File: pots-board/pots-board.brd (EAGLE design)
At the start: 160 x 100 mm, 29 parts

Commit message: mods
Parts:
- renumbered A to POT1, B to POT2, C to POT3, D to POT4, E to POT5
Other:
- board text added: "hotchk155"
- board text added: "meta-step pots board rev 1"
- board text added: "six4pix.com/metastep"

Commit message: reverse order
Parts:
- moved VCC 125.1 mm to (14.0, 61.0)
- moved GND 124.5 mm to (14.0, 43.2)
- moved GND40 124.5 mm to (14.0, 45.7)
- moved VA 124.5 mm to (14.0, 58.4)
- moved VB 124.5 mm to (14.0, 55.9)
- moved VC 124.5 mm to (14.0, 53.3)
- moved VD 124.5 mm to (14.0, 50.8)
- moved VE 124.5 mm to (14.0, 48.3)
- moved VC1 12.7 mm to (16.5, 61.0)
- moved VCC10 12.7 mm to (135.9, 61.0)
- moved XD 2.54 mm to (16.5, 50.8)
- moved YD 2.54 mm to (135.9, 50.8)
- moved XA 2.54 mm to (16.5, 58.4)
- moved XB 2.54 mm to (16.5, 55.9)
- moved XC 2.54 mm to (16.5, 53.3)
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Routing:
- net N$3: track 139.5 -> 14.8 mm, vias 2 -> 0
- net N$7: track 42.7 -> 127.3 mm, vias 2 -> 1
- net N$4: track 112.9 -> 42.6 mm
- net N$1: track 189.1 -> 136.5 mm, vias 5 -> 0
- net N$6: track 59.9 -> 100.8 mm, vias 2 -> 1
- net N$5: track 85.3 -> 67.2 mm, vias 2 -> 1
- net N$10: track 119.4 -> 121.8 mm, vias 0 -> 1
- net N$8: track 122.5 -> 120.1 mm
- net GND: track 1.27 -> 0.00 mm
- net N$11: track 121.0 -> 120.4 mm, vias 0 -> 1
- net N$9: track 121.0 -> 120.4 mm
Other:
- outline, holes or cut-outs redrawn
- board text added: "1"
- board text added: "2"
- board text added: "3"
- board text added: "4"
- board text added: "5"
- board text added: "VCC A1 A2 A3 A4 A5 GND GND"
- board text added: "VCC B1 B2 B3 B4 B5 GND GND"

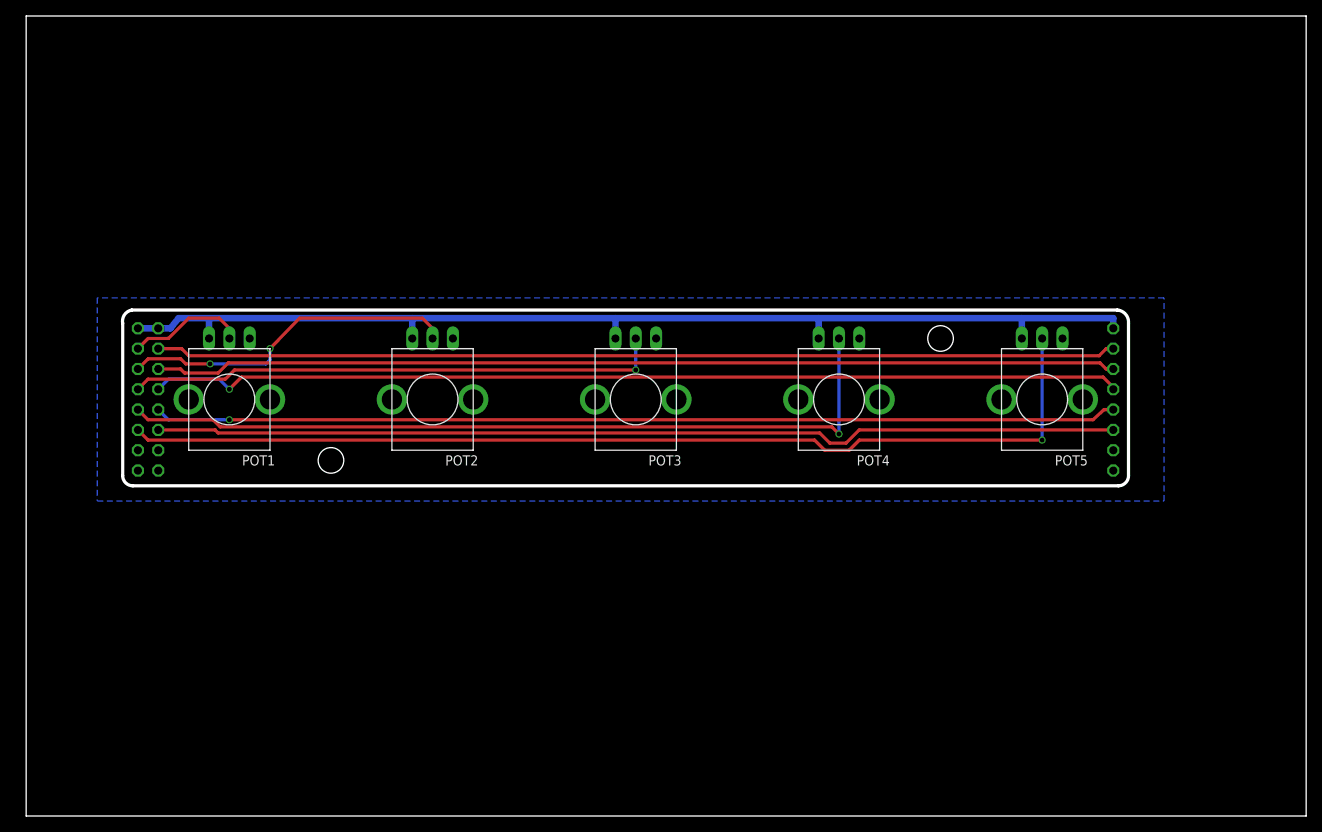
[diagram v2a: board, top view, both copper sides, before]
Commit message: pos
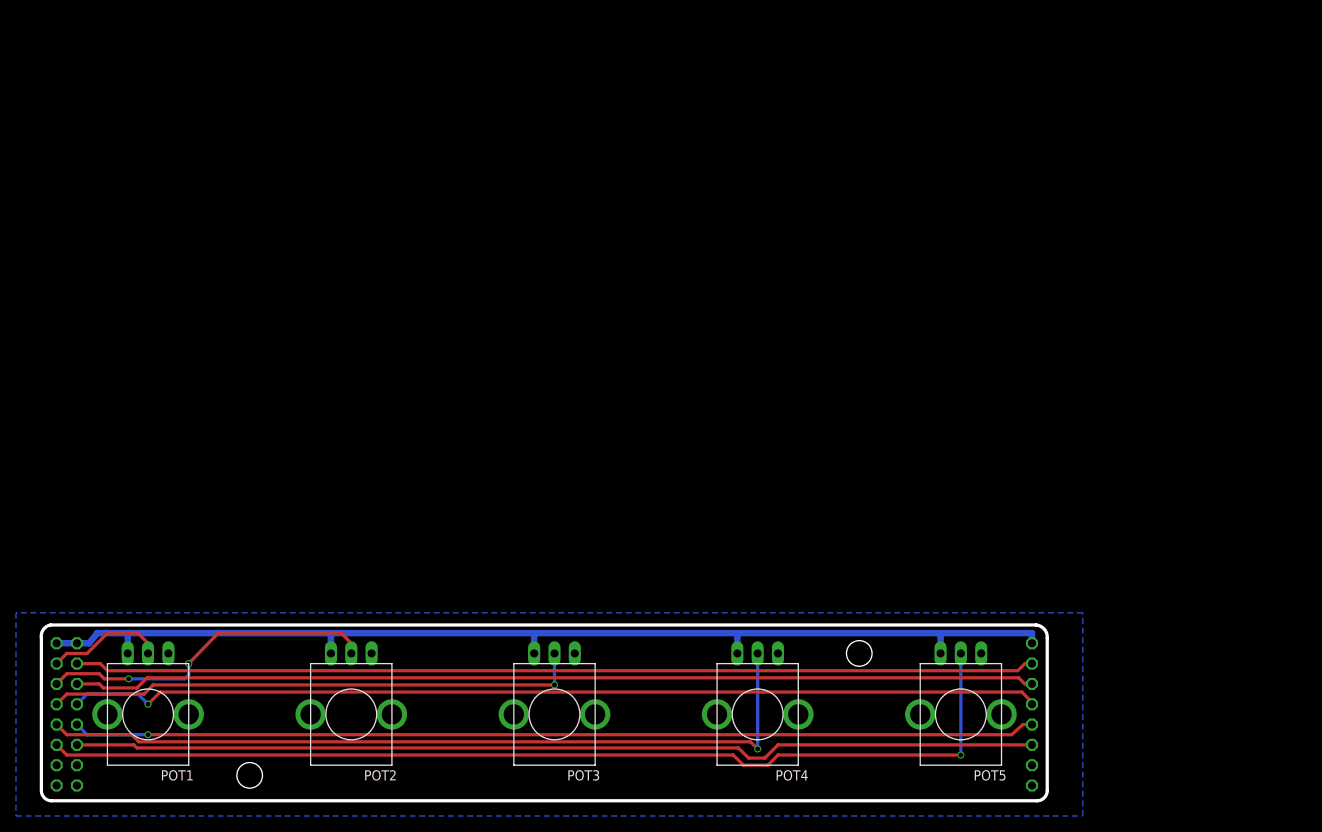
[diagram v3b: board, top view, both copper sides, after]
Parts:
- moved POT1 40.7 mm to (15.2, 12.7)
- moved POT2 40.7 mm to (40.6, 12.7)
- moved POT3 40.7 mm to (66.0, 12.7)
- moved POT4 40.7 mm to (91.4, 12.7)
- moved POT5 40.7 mm to (116.8, 12.7)
- moved VA 40.7 mm to (3.81, 19.1)
- moved VB 40.7 mm to (3.81, 16.5)
- moved VC 40.7 mm to (3.81, 14.0)
- moved VC1 40.7 mm to (6.35, 21.6)
- moved VCC 40.7 mm to (3.81, 21.6)
- moved XA 40.7 mm to (6.35, 19.1)
- moved XB 40.7 mm to (6.35, 16.5)
- moved XC 40.7 mm to (6.35, 14.0)
- moved GD1 40.7 mm to (6.35, 6.35)
- moved GD2 40.7 mm to (6.35, 3.81)
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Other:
- board size 160 x 100 mm -> 125.8 x 22 mm

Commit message: stuff
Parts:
- added C1, C2, C3, C4: (no value), rcl:C0805
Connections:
- removed net N$1: POT1.B, POT2.B, POT3.B, POT4.B, POT5.B, VC1.1, VCC.1, VCC10.1
- new net VCC: C1.1, C2.1, C3.1, C4.1, POT1.B, POT2.B, POT3.B, POT4.B, POT5.B, VC1.1, VCC.1, VCC10.1
- net GND: now also C1.2, C2.2, C3.2, C4.2
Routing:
- net VCC: track 0.00 -> 147.9 mm
- net N$1: track 136.5 -> 0.00 mm
- net GND: track 0.00 -> 30.6 mm, vias 0 -> 3
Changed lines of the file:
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@@
 <attribute name="VALUE" x="127" y="18.415" size="1.27" layer="28" rot="MR0"/>
+</element>
+<element name="C1" library="rcl" package="C0805" value="" x="34.29" y="20.32" smashed="yes" rot="R180">
+<attribute name="NAME" x="34.671" y="19.05" size="1.27" layer="25" rot="R180"/>
+<attribute name="VALUE" x="35.56" y="22.86" size="1.27" layer="27" rot="R180"/>
+</element>
+<element name="C2" library="rcl" package="C0805" value="" x="59.69" y="20.32" smashed="yes" rot="R180">
+<attribute name="NAME" x="59.817" y="19.05" size="1.27" layer="25" rot="R180"/>
+<attribute name="VALUE" x="60.96" y="22.86" size="1.27" layer="27" rot="R180"/>
+</element>
+<element name="C3" library="rcl" package="C0805" value="" x="85.09" y="20.32" smashed="yes" rot="R180">
+<attribute name="NAME" x="85.217" y="19.05" size="1.27" layer="25" rot="R180"/>
+<attribute name="VALUE" x="86.36" y="22.86" size="1.27" layer="27" rot="R180"/>
+</element>
+<element name="C4" library="rcl" package="C0805" value="" x="110.49" y="20.32" smashed="yes" rot="R180">
+<attribute name="NAME" x="110.617" y="19.05" size="1.27" layer="25" rot="R180"/>
+<attribute name="VALUE" x="111.76" y="22.86" size="1.27" layer="27" rot="R180"/>
 </element>
 </elements>
 <signals>
-<signal name="N$1">
+<signal name="VCC">
 <contactref element="VC1" pad="1"/>
 <contactref element="POT5" pad="B"/>
@@
 <wire x1="88.9" y1="20.32" x2="88.9" y2="22.86" width="0.8128" layer="16"/>
 <wire x1="114.3" y1="20.32" x2="114.3" y2="22.86" width="0.8128" layer="16"/>
+<contactref element="C1" pad="1"/>
+<contactref element="C4" pad="1"/>
+<contactref element="C3" pad="1"/>
+<contactref element="C2" pad="1"/>
+<wire x1="60.64" y1="20.32" x2="63.5" y2="20.32" width="0.4064" layer="1"/>
+<wire x1="35.24" y1="20.32" x2="38.1" y2="20.32" width="0.4064" layer="1"/>
+<wire x1="88.9" y1="20.32" x2="86.04" y2="20.32" width="0.4064" layer="1"/>
+<wire x1="114.3" y1="20.32" x2="111.44" y2="20.32" width="0.4064" layer="1"/>
 </signal>
 <signal name="N$3">
@@
 <contactref element="GND50" pad="1"/>
 <contactref element="GND40" pad="1"/>
+<contactref element="C1" pad="2"/>
+<contactref element="C4" pad="2"/>
+<contactref element="C2" pad="2"/>
+<contactref element="C3" pad="2"/>
+<wire x1="33.34" y1="20.32" x2="31.75" y2="20.32" width="0.4064" layer="1"/>
+<via x="31.75" y="20.32" extent="1-16" drill="0.6"/>
+<wire x1="31.75" y1="20.32" x2="24.13" y2="19.05" width="0.4064" layer="16"/>
+<wire x1="109.54" y1="20.32" x2="107.95" y2="20.32" width="0.4064" layer="1"/>
+<via x="107.95" y="20.32" extent="1-16" drill="0.6"/>
+<wire x1="107.95" y1="20.32" x2="106.68" y2="20.32" width="0.4064" layer="16"/>
+<wire x1="84.14" y1="20.32" x2="82.55" y2="20.32" width="0.4064" layer="1"/>
+<via x="82.55" y="20.32" extent="1-16" drill="0.6"/>
+<wire x1="82.55" y1="20.32" x2="82.55" y2="19.05" width="0.4064" layer="16"/>
+<wire x1="58.74" y1="20.32" x2="43.18" y2="20.32" width="0.4064" layer="1"/>
 </signal>
 </signals>
